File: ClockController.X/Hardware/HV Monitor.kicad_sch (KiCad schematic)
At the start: 2 parts

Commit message: Updated most footprints
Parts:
- R3, R4: footprint Clock Controller:RES_0805 -> Resistor_SMD:R_0805_2012Metric
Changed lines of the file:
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@@
 			)
 		)
-		(property "Footprint" "Clock Controller:RES_0805"
+		(property "Footprint" "Resistor_SMD:R_0805_2012Metric"
 			(at 102.87 87.63 0)
 			(effects
@@
 			)
 		)
-		(property "Footprint" "Clock Controller:RES_0805"
+		(property "Footprint" "Resistor_SMD:R_0805_2012Metric"
 			(at 102.87 115.57 0)
 			(effects

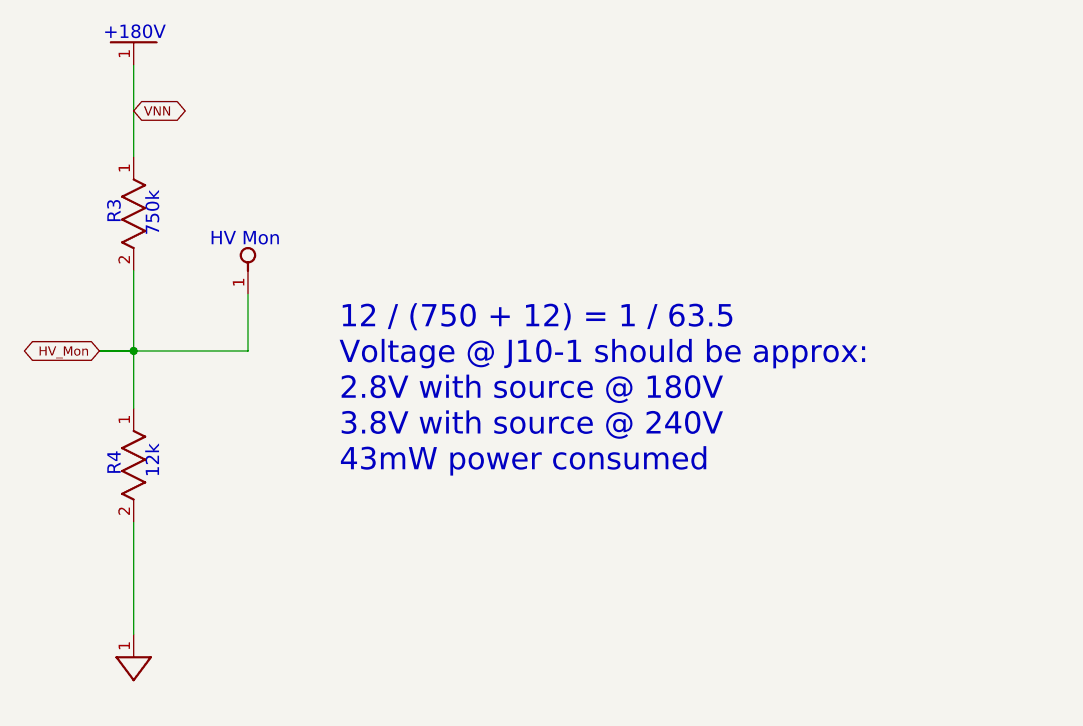
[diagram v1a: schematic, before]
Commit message: More frequent ADC polling and over-voltage protection
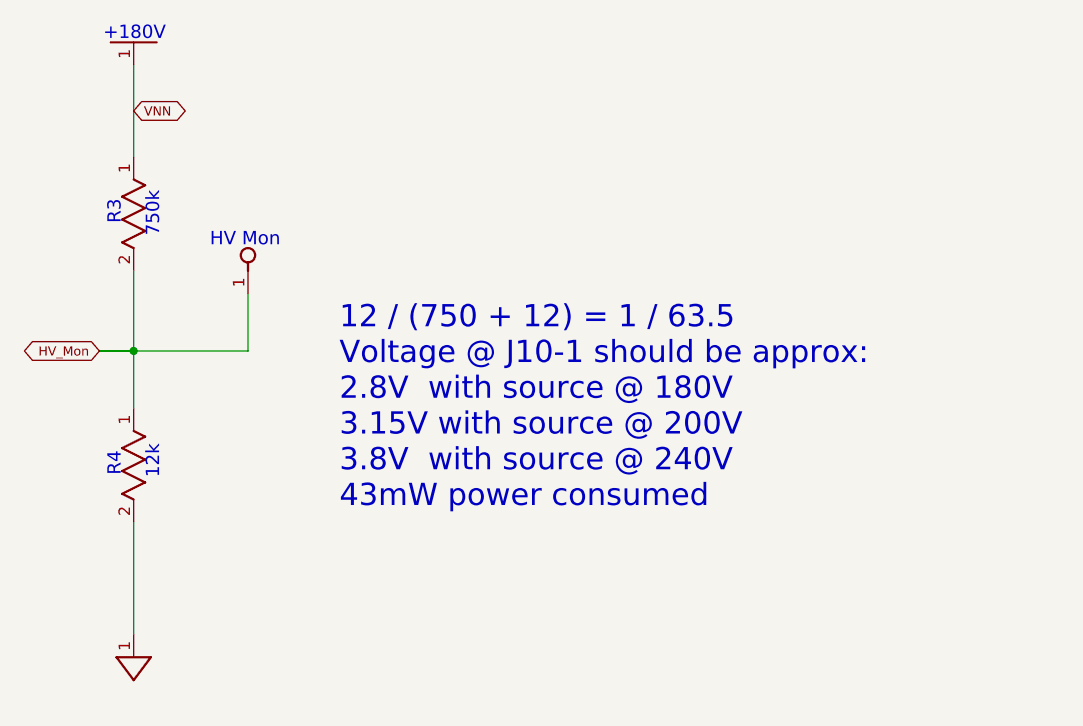
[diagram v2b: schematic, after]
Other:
- note added: "12 / (750 + 12) = 1 / 63.5 Voltage @ J10-1 should be approx: 2.8V with source @ 180V 3.15V with source @ 200V 3.8V with source @ 240V 43mW power consumed"
- note removed: "12 / (750 + 12) = 1 / 63.5 Voltage @ J10-1 should be approx: 2.8V with source @ 180V 3.8V with source @ 240V 43mW power consumed"
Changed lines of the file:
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@@
 		)
 	)
-	(text "12 / (750 + 12) = 1 / 63.5\nVoltage @ J10-1 should be approx:\n2.8V with source @ 180V\n3.8V with source @ 240V\n43mW power consumed"
+	(text "12 / (750 + 12) = 1 / 63.5\nVoltage @ J10-1 should be approx:\n2.8V  with source @ 180V\n3.15V with source @ 200V\n3.8V  with source @ 240V\n43mW power consumed"
 		(exclude_from_sim no)
 		(at 125.73 97.79 0)

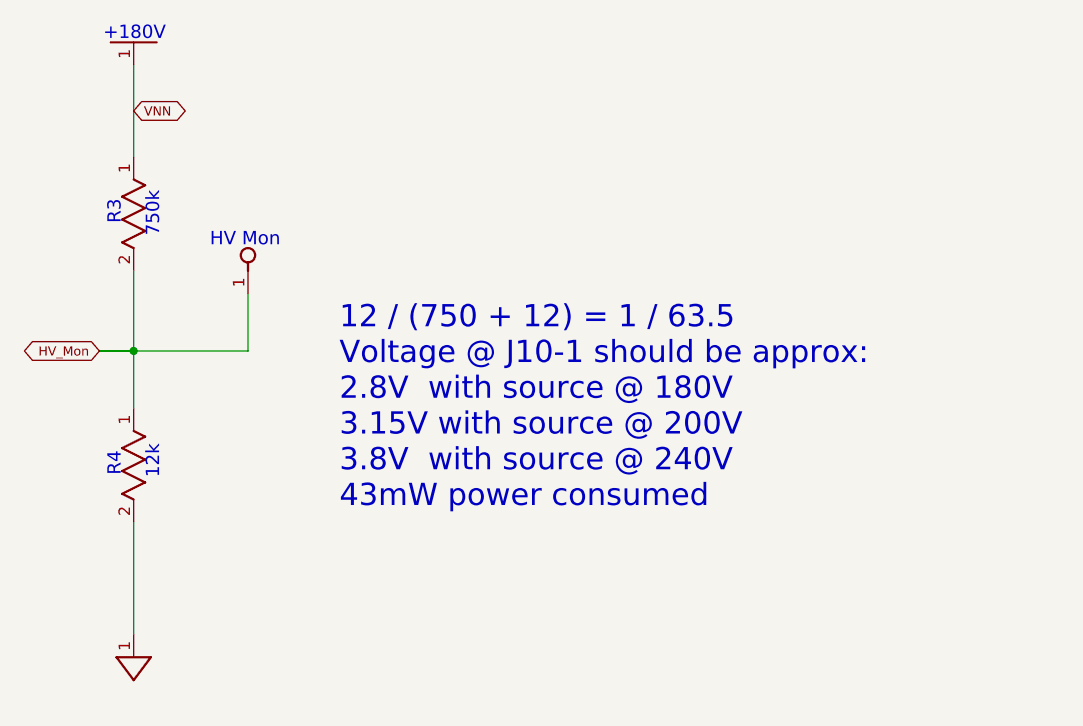
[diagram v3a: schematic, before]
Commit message: Replace the imported objects with native kicad equivalents
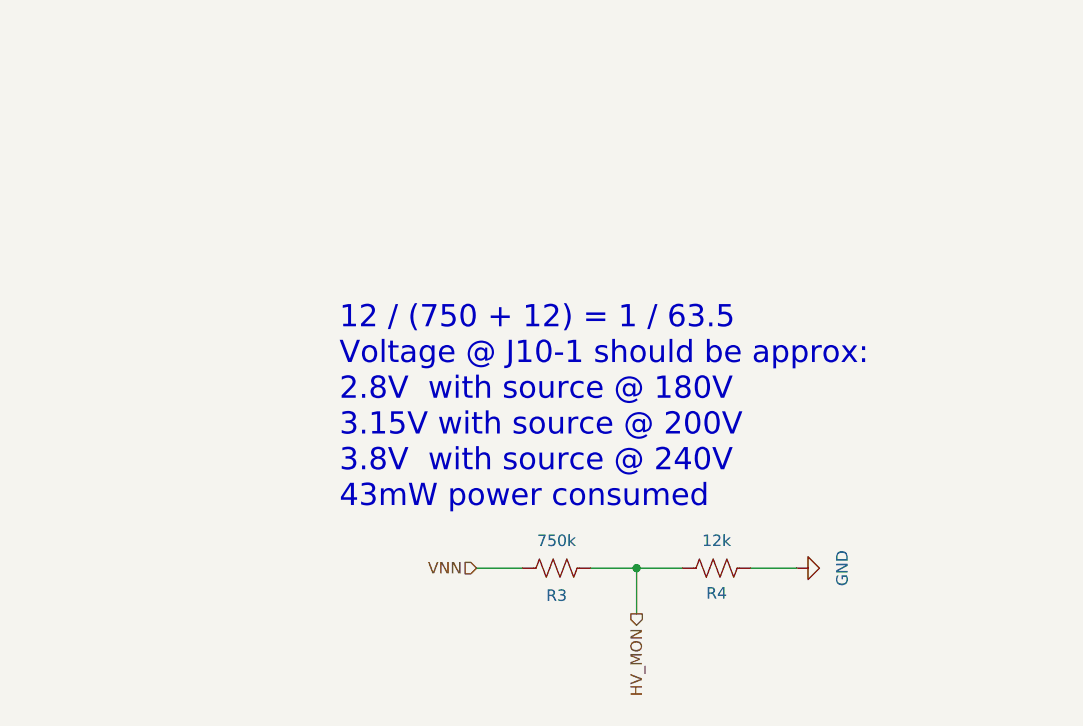
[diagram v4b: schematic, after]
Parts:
- R3, R4: symbol Clock Controller-eagle-import:RES_0805 -> Device:R_US
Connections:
- net +180V is gone; now on net HV_MON: R3.1
- net GND_DIGITAL is gone; now on net HV_MON: R4.2
- net HV_MON: no longer R3.2, R4.1
- new net GND: R4.1
- new net VNN: R3.2
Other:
- note removed: "+180V"
- note removed: "12k"
- note removed: "750k"
- note removed: "HV Mon"
- note removed: "R3"
- note removed: "R4"

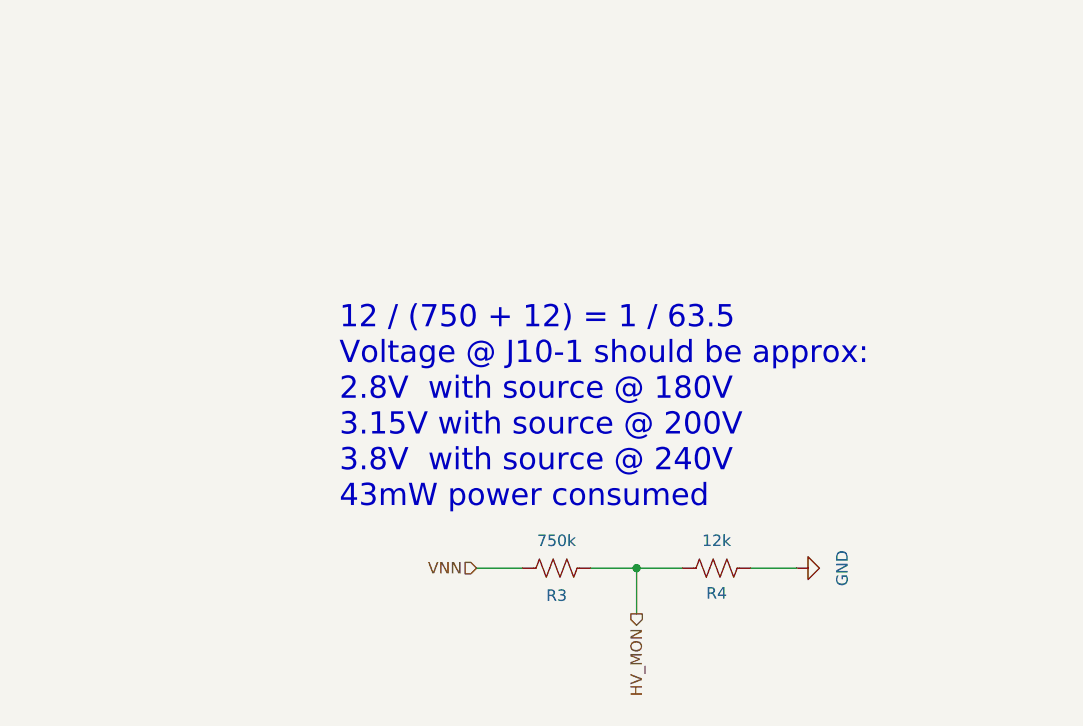
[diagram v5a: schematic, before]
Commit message: Converting to single board layout
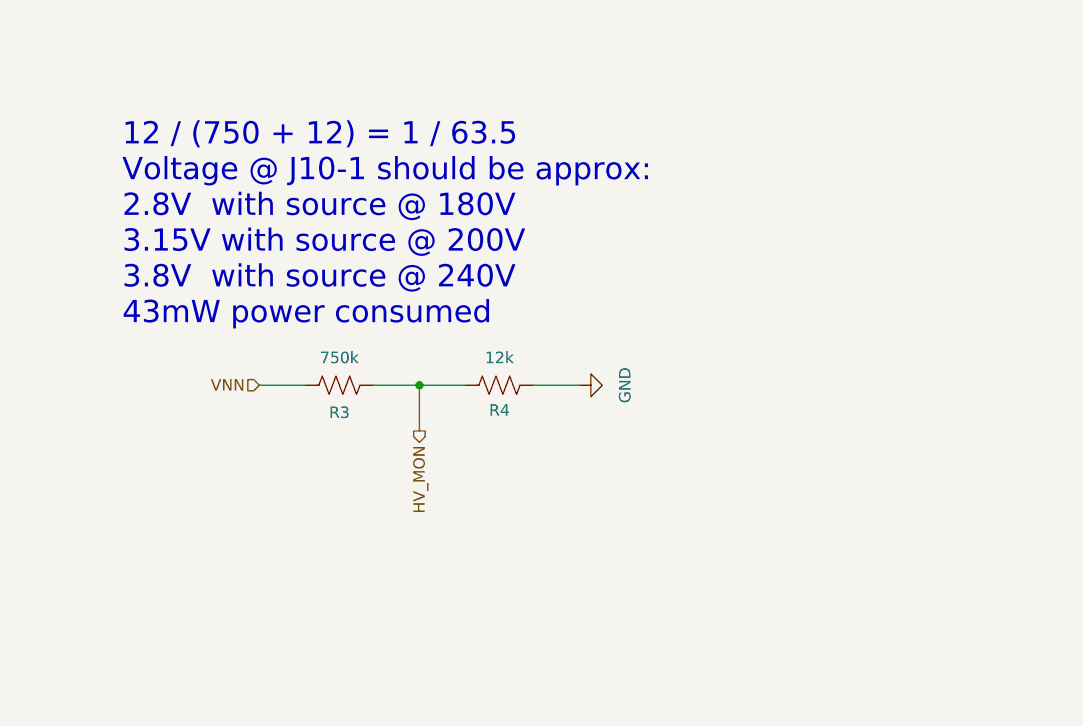
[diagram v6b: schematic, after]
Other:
- moved on the sheet: R3, R4
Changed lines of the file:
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@@
 	(generator "eeschema")
 	(generator_version "9.0")
-	(paper "A4")
+	(paper "USLetter")
 	(text "12 / (750 + 12) = 1 / 63.5\nVoltage @ J10-1 should be approx:\n2.8V  with source @ 180V\n3.15V with source @ 200V\n3.8V  with source @ 240V\n43mW power consumed"
 		(exclude_from_sim no)
-		(at 125.73 97.79 0)
+		(at 101.6 77.47 0)
 		(effects
 			(font
@@
 	)
 	(junction
-		(at 158.75 127)
+		(at 134.62 106.68)
 		(diameter 0)
 		(color 0 0 0 0)
@@
 	(wire
 		(pts
-			(xy 158.75 127) (xy 163.83 127)
-		)
-		(stroke
-			(width 0)
-			(type default)
-		)
-	)
-	(wire
-		(pts
-			(xy 153.67 127) (xy 158.75 127)
-		)
-		(stroke
-			(width 0)
-			(type default)
-		)
-	)
-	(wire
-		(pts
-			(xy 158.75 132.08) (xy 158.75 127)
-		)
-		(stroke
-			(width 0)
-			(type default)
-		)
-	)
-	(wire
-		(pts
-			(xy 140.97 127) (xy 146.05 127)
-		)
-		(stroke
-			(width 0)
-			(type default)
-		)
-	)
-	(wire
-		(pts
-			(xy 176.53 127) (xy 171.45 127)
+			(xy 134.62 106.68) (xy 139.7 106.68)
+		)
+		(stroke
+			(width 0)
+			(type default)
+		)
+	)
+	(wire
+		(pts
+			(xy 129.54 106.68) (xy 134.62 106.68)
+		)
+		(stroke
+			(width 0)
+			(type default)
+		)
+	)
+	(wire
+		(pts
+			(xy 134.62 111.76) (xy 134.62 106.68)
+		)
+		(stroke
+			(width 0)
+			(type default)
+		)
+	)
+	(wire
+		(pts
+			(xy 116.84 106.68) (xy 121.92 106.68)
+		)
+		(stroke
+			(width 0)
+			(type default)
+		)
+	)
+	(wire
+		(pts
+			(xy 152.4 106.68) (xy 147.32 106.68)
 		)
 		(stroke
@@
 	(hierarchical_label "VNN"
 		(shape input)
-		(at 140.97 127 180)
+		(at 116.84 106.68 180)
 		(effects
 			(font
@@
 	(hierarchical_label "HV_MON"
 		(shape output)
-		(at 158.75 132.08 270)
+		(at 134.62 111.76 270)
 		(effects
 			(font
@@
 	(symbol
 		(lib_id "Device:R_US")
-		(at 149.86 127 270)
+		(at 125.73 106.68 270)
 		(unit 1)
 		(exclude_from_sim no)
@@
 		(dnp no)
 		(property "Reference" "R3"
-			(at 149.86 130.048 90)
+			(at 125.73 109.728 90)
 			(effects
 				(font
@@
 		)
 		(property "Value" "750k"
-			(at 149.86 123.952 90)
+			(at 125.73 103.632 90)
 			(effects
 				(font
@@
 		)
 		(property "Footprint" "Resistor_SMD:R_0805_2012Metric"
-			(at 149.606 128.016 90)
+			(at 125.476 107.696 90)
 			(effects
 				(font
@@
 		)
 		(property "Datasheet" "~"
-			(at 149.86 127 0)
+			(at 125.73 106.68 0)
 			(effects
 				(font
@@
 		)
 		(property "Description" "Resistor, US symbol"
-			(at 149.86 127 0)
+			(at 125.73 106.68 0)
 			(effects
 				(font
@@
 	(symbol
 		(lib_id "power:GND")
-		(at 176.53 127 90)
+		(at 152.4 106.68 90)
 		(unit 1)
 		(exclude_from_sim no)
@@
 		(fields_autoplaced yes)
 		(property "Reference" "#PWR016"
-			(at 182.88 127 0)
+			(at 158.75 106.68 0)
 			(effects
 				(font
@@
 		)
 		(property "Value" "GND"
-			(at 181.61 127 0)
+			(at 157.48 106.68 0)
 			(effects
 				(font
@@
 		)
 		(property "Footprint" ""
-			(at 176.53 127 0)
+			(at 152.4 106.68 0)
 			(effects
 				(font
@@
 		)
 		(property "Datasheet" ""
-			(at 176.53 127 0)
+			(at 152.4 106.68 0)
 			(effects
 				(font
@@
 		)
 		(property "Description" "Power symbol creates a global label with name \"GND\" , ground"
-			(at 176.53 127 0)
+			(at 152.4 106.68 0)
 			(effects
 				(font
@@
 	(symbol
 		(lib_id "Device:R_US")
-		(at 167.64 127 270)
+		(at 143.51 106.68 270)
 		(unit 1)
 		(exclude_from_sim no)
@@
 		(dnp no)
 		(property "Reference" "R4"
-			(at 167.64 129.794 90)
+			(at 143.51 109.474 90)
 			(effects
 				(font
@@
 		)
 		(property "Value" "12k"
-			(at 167.64 123.952 90)
+			(at 143.51 103.632 90)
 			(effects
 				(font
@@
 		)
 		(property "Footprint" "Resistor_SMD:R_0805_2012Metric"
-			(at 167.386 128.016 90)
+			(at 143.256 107.696 90)
 			(effects
 				(font
@@
 		)
 		(property "Datasheet" "~"
-			(at 167.64 127 0)
+			(at 143.51 106.68 0)
 			(effects
 				(font
@@
 		)
 		(property "Description" "Resistor, US symbol"
-			(at 167.64 127 0)
-			(effects
-				(font
+			(at 143.51 106.68 0)
+			(effects
+				(font
